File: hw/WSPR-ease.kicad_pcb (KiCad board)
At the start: 4 copper layers, 99 x 64 mm, 127 parts, among them J101 pwr+data, J102 SMA, J103 SMA, K201 G6K-2, K202 G6K-2, K203 G6K-2, Q101 MMBF170, Q201 MMBF170, Q202 MMBF170, Q203 MMBF170, Q301 MMBF170, Q302 MMBF170, Q303 MMBF170, Q304 MMBF170, Q305 MMBF170, Q306 MMBF170, Q307 MMBF170, Q308 MMBF170, T301 BN-43-202_DualPri_CTSec, U101 SRV05-4, U102 ESP32-S3-WROOM-1-N8R8, U103 LMR51430YDDCR, U104 GNSS module, U301 SN74LVC1G74DCTR, U302 UCC27525DGN, U303 UCC27525DGN, U304 Si5351C-B-GM1, Y301 40MHz

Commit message: Now using RP2040 as a DDS. I can use SPI co-host to program its (SPI) flash. I can use I2C between ESP32 and RP2040 to send commands and receive status.
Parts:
- removed the C304 at (81.4, 115.0)
- removed the C306 at (80.9, 113.7)
- removed the R302 at (77.1, 113.0)
- removed the U301 at (85.4, 113.0)
- added C401: 1uF X5R 25V, Capacitor_SMD:C_0402_1005Metric, F.Cu at (104.3, 108.5)
- added C402: 100nF X7R 50V, Capacitor_SMD:C_0402_1005Metric, F.Cu at (105.3, 108.5)
- added C403: 100pF NP0 50V, Capacitor_SMD:C_0402_1005Metric, F.Cu at (106.3, 108.5)
- added C404: 1uF X5R 25V, Capacitor_SMD:C_0402_1005Metric, F.Cu at (107.0, 102.2)
- added C405: 100nF X7R 50V, Capacitor_SMD:C_0402_1005Metric, F.Cu at (108.0, 102.2)
- added C406: 100nF X7R 50V, Capacitor_SMD:C_0402_1005Metric, F.Cu at (94.6, 98.3)
- added C407: 56pF NP0 50V, Capacitor_SMD:C_0402_1005Metric, F.Cu at (83.2, 97.0)
- added C408: 82pF NP0 50V, Capacitor_SMD:C_0402_1005Metric, F.Cu at (83.2, 94.8)
- added C409: 56pF NP0 50V, Capacitor_SMD:C_0402_1005Metric, F.Cu at (94.7, 100.5)
- added C410: 100nF X7R 50V, Capacitor_SMD:C_0402_1005Metric, F.Cu at (72.8, 109.5)
- added C411: 100nF X7R 50V, Capacitor_SMD:C_0402_1005Metric, F.Cu at (83.2, 108.6)
- added C412: 1uF X5R 25V, Capacitor_SMD:C_0402_1005Metric, F.Cu at (83.2, 111.2)
- added C413: 1uF X5R 25V, Capacitor_SMD:C_0402_1005Metric, F.Cu at (83.2, 112.1)
- added C414: 100nF X7R 50V, Capacitor_SMD:C_0402_1005Metric, F.Cu at (81.5, 104.0)
- added C415: 100nF X7R 50V, Capacitor_SMD:C_0402_1005Metric, F.Cu at (77.0, 103.7)
- added C416: 100nF X7R 50V, Capacitor_SMD:C_0402_1005Metric, F.Cu at (73.0, 108.5)
- added C417: 100nF X7R 50V, Capacitor_SMD:C_0402_1005Metric, F.Cu at (77.0, 113.8)
- added C418: 100nF X7R 50V, Capacitor_SMD:C_0402_1005Metric, F.Cu at (80.2, 113.8)
- added C419: 100nF X7R 50V, Capacitor_SMD:C_0402_1005Metric, F.Cu at (81.5, 113.5)
- added C420: 100nF X7R 50V, Capacitor_SMD:C_0402_1005Metric, F.Cu at (83.2, 110.2)
- added C421: 100nF X7R 50V, Capacitor_SMD:C_0402_1005Metric, F.Cu at (83.9, 117.0)
- added FB401: 600, Inductor_SMD:L_0603_1608Metric, F.Cu at (105.7, 106.8)
- added L401: 1.2uH, Inductor_SMD:L_1008_2520Metric, F.Cu at (85.5, 95.9)
- added L402: 1.2uH, Inductor_SMD:L_1008_2520Metric, F.Cu at (92.2, 100.3)
- added R401: 22.1k, Resistor_SMD:R_0402_1005Metric, F.Cu at (104.9, 105.0)
- added R402: 100, Resistor_SMD:R_0402_1005Metric, F.Cu at (75.0, 98.4)
- added R403: 100, Resistor_SMD:R_0402_1005Metric, F.Cu at (76.9, 98.4)
- added R404: 100, Resistor_SMD:R_0402_1005Metric, F.Cu at (78.8, 98.4)
- added R405: 100, Resistor_SMD:R_0402_1005Metric, F.Cu at (80.7, 98.4)
- added R406: 100, Resistor_SMD:R_0402_1005Metric, F.Cu at (82.6, 98.4)
- added R407: 100, Resistor_SMD:R_0402_1005Metric, F.Cu at (84.5, 98.4)
- added R408: 100, Resistor_SMD:R_0402_1005Metric, F.Cu at (86.4, 98.4)
- added R409: 200, Resistor_SMD:R_0402_1005Metric, F.Cu at (75.5, 100.7)
- added R410: 200, Resistor_SMD:R_0402_1005Metric, F.Cu at (76.5, 100.7)
- added R411: 200, Resistor_SMD:R_0402_1005Metric, F.Cu at (77.5, 100.7)
- added R412: 200, Resistor_SMD:R_0402_1005Metric, F.Cu at (78.5, 100.7)
- added R413: 200, Resistor_SMD:R_0402_1005Metric, F.Cu at (79.5, 100.7)
- added R414: 200, Resistor_SMD:R_0402_1005Metric, F.Cu at (80.5, 100.7)
- added R415: 200, Resistor_SMD:R_0402_1005Metric, F.Cu at (81.5, 100.7)
- added R416: 200, Resistor_SMD:R_0402_1005Metric, F.Cu at (82.5, 100.7)
- added R417: 200, Resistor_SMD:R_0402_1005Metric, F.Cu at (83.5, 100.7)
- added R418: 200, Resistor_SMD:R_0402_1005Metric, F.Cu at (92.7, 98.3)
- added R419: 22.1k, Resistor_SMD:R_0402_1005Metric, F.Cu at (104.9, 103.1)
- added TP401: GPIO8, TestPoint:TestPoint_Pad_1.5x1.5mm, F.Cu at (73.0, 103.3)
- added TP402: SWDIO, TestPoint:TestPoint_Bridge_Pitch2.0mm_Drill0.7mm, F.Cu at (76.0, 120.3)
- added TP403: SWCLK, TestPoint:TestPoint_Bridge_Pitch2.0mm_Drill0.7mm, F.Cu at (73.5, 120.3)
- added U401: 74LVC1G04, Package_TO_SOT_SMD:SOT-553, F.Cu at (106.6, 104.2)
- added U402: RP2040, Package_DFN_QFN:QFN-56-1EP_7x7mm_P0.4mm_EP3.2x3.2mm, F.Cu at (78.0, 108.8)
- added U403: W25Q128JVS, Package_SO:SOIC-8_5.3x5.3mm_P1.27mm, F.Cu at (89.5, 115.1)
- C101, C103, C110, C205, C206, C207, C208, C209, C210, C211, C212, C302, C307, C309: footprint Capacitor_SMD:C_0603_1608Metric -> Capacitor_SMD:C_0402_1005Metric
- C108, C303, C308: value 100pF NP0 100V -> 100pF NP0 50V; footprint Capacitor_SMD:C_0603_1608Metric -> Capacitor_SMD:C_0402_1005Metric
- C201, C204: value 910pF NP0 100V -> 910pF NP0 50V; footprint Capacitor_SMD:C_0603_1608Metric -> Capacitor_SMD:C_0402_1005Metric
- C202, C203: value 1.6nF NP0 63V -> 1.6nF NP0 25V; footprint Capacitor_SMD:C_0603_1608Metric -> Capacitor_SMD:C_0402_1005Metric
- C305: renamed from C312; footprint Capacitor_SMD:C_0603_1608Metric -> Capacitor_SMD:C_0402_1005Metric
- C312: renamed from C316; footprint Capacitor_SMD:C_0603_1608Metric -> Capacitor_SMD:C_0402_1005Metric
- C317: renamed from C319; footprint Capacitor_SMD:C_0603_1608Metric -> Capacitor_SMD:C_0402_1005Metric
- C319: renamed from C321; footprint Capacitor_SMD:C_0603_1608Metric -> Capacitor_SMD:C_0402_1005Metric
- C321: renamed from C323; footprint Capacitor_SMD:C_0603_1608Metric -> Capacitor_SMD:C_0402_1005Metric
- C323: renamed from C325; footprint Capacitor_SMD:C_0603_1608Metric -> Capacitor_SMD:C_0402_1005Metric
- C325: renamed from C327; footprint Capacitor_SMD:C_0603_1608Metric -> Capacitor_SMD:C_0402_1005Metric
- Y301: value 40MHz -> 12MHz; footprint Library:ECSTXO201633400TR -> Library:Oscillator_SMD_AbraconATX-H12-4Pin_2.5x2.0mm
- moved C304 26.2 mm to (73.1, 95.9)
- moved C305 26.2 mm to (74.4, 95.3)
- moved Y301 26.2 mm to (72.5, 98.8)
- moved R103 12.0 mm to (61.9, 125.7)
- moved R104 11.5 mm to (60.2, 126.1)
- moved C106 11.1 mm to (59.2, 126.1)
- moved R305 4.78 mm to (90.4, 109.8)
- moved R306 4.78 mm to (90.4, 108.5)
- moved C318 4.60 mm to (91.9, 104.6)
- moved C317 4.30 mm to (92.9, 104.6)
- moved C325 4.28 mm to (94.4, 104.4)
- moved C324 4.27 mm to (95.9, 111.2)
- moved C319 4.27 mm to (97.3, 108.5)
- moved C320 4.27 mm to (96.7, 109.8)
- moved C321 4.27 mm to (97.4, 106.7)
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- renumbered C311 to C304, C305 to C306, C313 to C311, C314 to C313, C315 to C314, C317 to C315, C318 to C316, C320 to C318, C322 to C320, C324 to C322, C326 to C324, C328 to C326, R303 to R302, R304 to R303, R305 to R304, R306 to R305, R307 to R306, U302 to U301, U303 to U302, U304 to U303
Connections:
- U102 pad 15: unconnected-(U102-IO3-Pad15) -> /ddsRUN
- U102 pad 18: /txCLKen -> unconnected-(U102-IO10-Pad18)
- U102 pad 19: /tcxoDiv2 -> /ddsClk
- U102 pad 22: unconnected-(U102-IO14-Pad22) -> /ddsSPI.D3
- U102 pad 23: unconnected-(U102-IO21-Pad23) -> /ddsSPI.SCK
- U102 pad 24: unconnected-(U102-IO47-Pad24) -> /ddsSPI.D0
- U102 pad 25: unconnected-(U102-IO48-Pad25) -> /ddsSPI.D2
- U102 pad 26: /ahcEn -> /ddsSPI.D1
- U102 pad 27: unconnected-(U102-IO0-Pad27) -> /ddsSPI.SS
- U102 pad 38: unconnected-(U102-IO2-Pad38) -> /ahcEn
- U303 pad 6: /Transmitter/tcxo -> /Transmitter/DDS/out
- Y301 pad 3: /Transmitter/tcxo -> /ddsClk
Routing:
- net /ddsSPI.D1: track 0.00 -> 38.3 mm, vias 0 -> 3
- net /ddsSPI.SS: track 0.00 -> 35.7 mm, vias 0 -> 3
- net /ddsSPI.D2: track 0.00 -> 32.1 mm, vias 0 -> 3
- net /ddsSPI.D0: track 0.00 -> 25.5 mm, vias 0 -> 3
- net /ddsSPI.D3: track 0.00 -> 24.5 mm, vias 0 -> 3
- net /ddsClk: track 0.00 -> 23.9 mm
- net /ddsSPI.SCK: track 0.00 -> 23.5 mm, vias 0 -> 3
- net +3.3V: track 46.0 -> 68.9 mm, vias 22 -> 32
- net /ahcEn: track 36.7 -> 58.8 mm, vias 0 -> 2
- net /Transmitter/DDS/out: track 0.00 -> 19.8 mm, vias 0 -> 2
- net Net-(C406-Pad2): track 0.00 -> 15.4 mm, vias 0 -> 2
- net /tcxoDiv2: track 15.0 -> 0.00 mm
- net /txCLKen: track 14.8 -> 0.00 mm
- net +1.1V: track 0.00 -> 14.0 mm
- net Net-(Q101-S): track 20.2 -> 6.68 mm
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
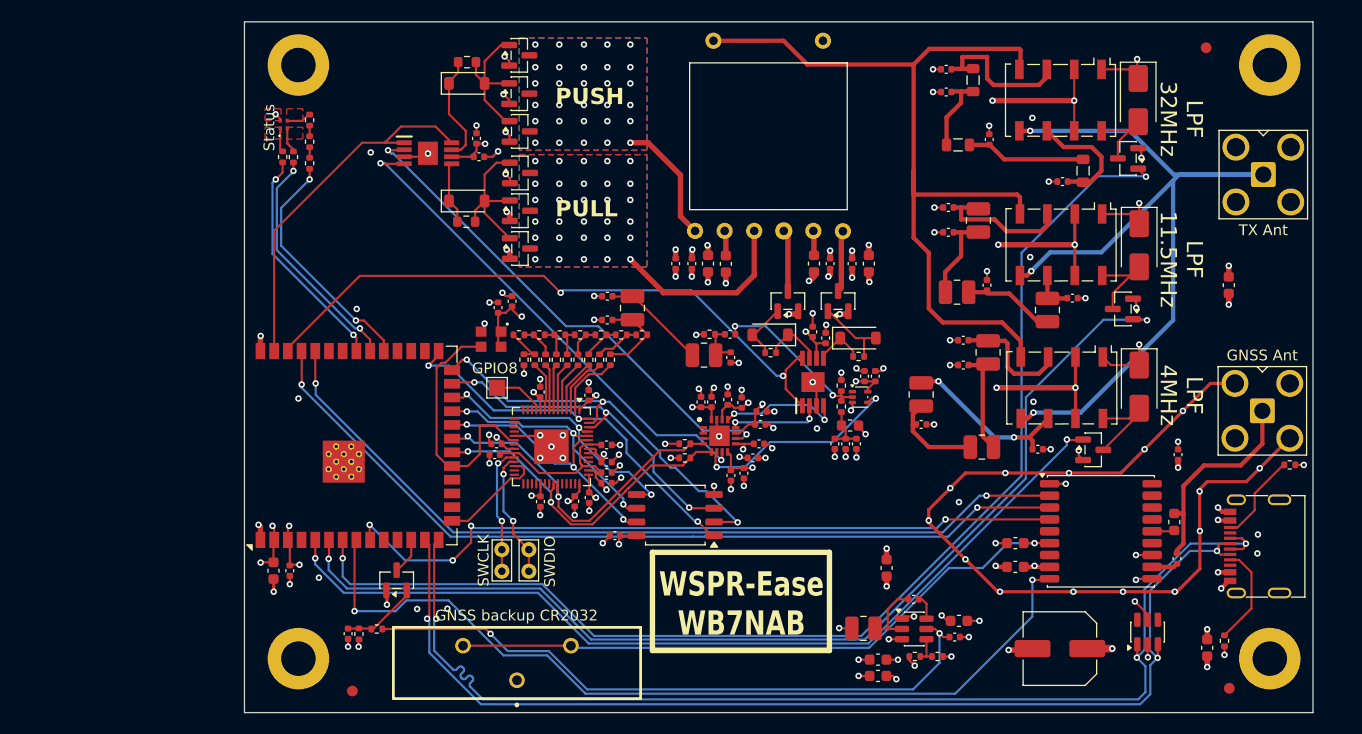
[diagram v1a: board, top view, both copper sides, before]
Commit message: Switched to SI5351 clocking MACHXO2 CPLD to drive gate driver for MOSFETs. It passes DRC but needs serious reviewing.
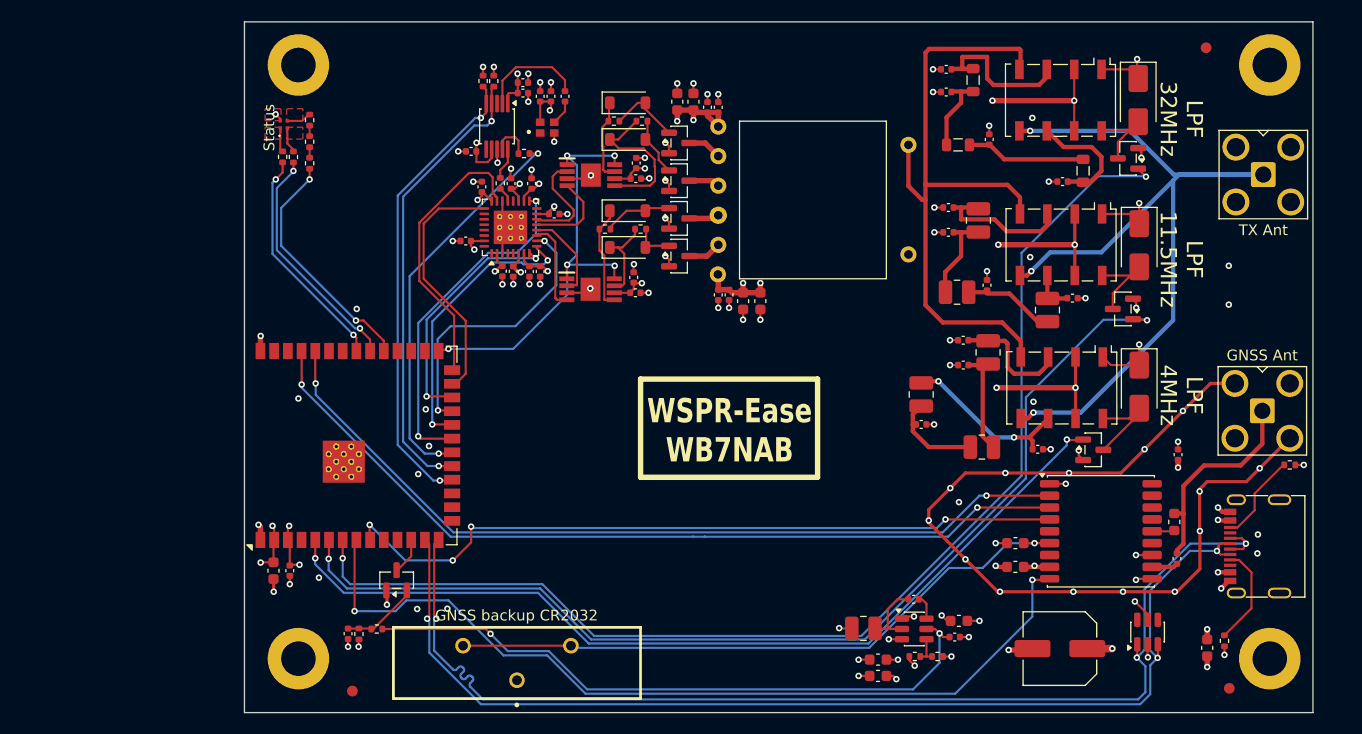
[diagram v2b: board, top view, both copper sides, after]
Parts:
- removed the C302 at (91.0, 91.8)
- removed the C305 at (74.4, 95.3)
- removed the C309 at (103.9, 91.8)
- removed C313, C314, C315, C316: 10uF X5R 25V, Capacitor_SMD:C_0603_1608Metric
- removed C317, C319, C321, C323, C325, C414, C419, C420, C421: 100nF X7R 50V, Capacitor_SMD:C_0402_1005Metric
- removed C318, C320, C322, C324, C326, C412, C413: 1uF X5R 25V, Capacitor_SMD:C_0402_1005Metric
- removed FB401: 600, Inductor_SMD:L_0603_1608Metric
- removed L401, L402: 1.2uH, Inductor_SMD:L_1008_2520Metric
- removed Q305, Q306, Q307, Q308: MMBF170, Package_TO_SOT_SMD:SOT-23
- removed R305, R306: 5.1k, Resistor_SMD:R_0402_1005Metric
- removed R405, R406, R407, R408: 100, Resistor_SMD:R_0402_1005Metric
- removed R409, R410, R411, R412, R413, R414, R415, R416, R417, R418: 200, Resistor_SMD:R_0402_1005Metric
- removed R419: 22.1k, Resistor_SMD:R_0402_1005Metric
- removed TP401: GPIO8, TestPoint:TestPoint_Pad_1.5x1.5mm
- removed TP402: SWDIO, TestPoint:TestPoint_Bridge_Pitch2.0mm_Drill0.7mm
- removed TP403: SWCLK, TestPoint:TestPoint_Bridge_Pitch2.0mm_Drill0.7mm
- removed U303: Si5351C-B-GM1, Library:QFN50P300X300X90-17N-D
- removed U403: W25Q128JVS, Package_SO:SOIC-8_5.3x5.3mm_P1.27mm
- removed Y301: 12MHz, Library:Oscillator_SMD_AbraconATX-H12-4Pin_2.5x2.0mm
- added C306: 100pF NP0 50V, Capacitor_SMD:C_0402_1005Metric, F.Cu at (93.5, 77.3)
- added C307: 100pF NP0 50V, Capacitor_SMD:C_0402_1005Metric, F.Cu at (93.5, 94.7)
- added C312: 10uF X5R 25V, Capacitor_SMD:C_0603_1608Metric, F.Cu at (95.8, 95.3)
- added Y401: 20MHz, Library:ECSTXO201633400TR, F.Cu at (77.7, 79.2)
- C303: value 100pF NP0 50V -> 10uF X5R 25V; footprint Capacitor_SMD:C_0402_1005Metric -> Capacitor_SMD:C_0603_1608Metric
- C304, C401, C404: value 1uF X5R 25V -> 100nF X7R 50V
- C308, C403: value 100pF NP0 50V -> 100nF X7R 50V
- C407: value 56pF NP0 50V -> 1uF X5R 25V
- C408: value 82pF NP0 50V -> 1uF X5R 25V
- C409: value 56pF NP0 50V -> 100nF X7R 50V
- C417: value 100nF X7R 50V -> 1uF X5R 25V
- D301, D302, D303, D304: value 1N4148W -> BAT54FILM
- Q101, Q201, Q202, Q203, Q301, Q302, Q303, Q304: value MMBF170 -> IRLML2060
- R301, R302: value 10 -> 27; footprint Resistor_SMD:R_0603_1608Metric -> Resistor_SMD:R_0402_1005Metric
- R303, R304: value 47 -> 27
- R401: value 22.1k -> 27
- R402, R403: value 100 -> 5.1k
- R404: value 100 -> 27
- U301, U302: value UCC27525DGN -> UCC27523DGN
- U401: value 74LVC1G04 -> LCMXO2-256HC-4SG32C; footprint Package_TO_SOT_SMD:SOT-553 -> Package_DFN_QFN:QFN-32-1EP_5x5mm_P0.5mm_EP3.1x3.1mm_ThermalVias
- U402: value RP2040 -> SI5351A-B-GT; footprint Package_DFN_QFN:QFN-56-1EP_7x7mm_P0.4mm_EP3.2x3.2mm -> Package_SO:MSOP-10_3x3mm_P0.5mm
- moved C402 39.9 mm to (70.1, 89.7), turned to 0 degrees
- moved C404 39.6 mm to (71.6, 84.7), turned to -90 degrees
- moved R401 37.8 mm to (73.3, 84.4), turned to 90 degrees
- moved C418 37.7 mm to (77.0, 76.3), turned to 90 degrees
- moved C417 37.6 mm to (78.0, 76.3), turned to 90 degrees
- moved C401 37.0 mm to (76.2, 84.4)
- moved C403 36.5 mm to (73.5, 92.5)
- moved U401 36.0 mm to (74.2, 88.4), turned to 90 degrees
- moved C405 33.5 mm to (76.0, 92.5)
- moved C409 31.2 mm to (75.4, 76.0), turned to 180 degrees
- moved U402 30.1 mm to (73.0, 79.1)
- moved C415 27.5 mm to (79.3, 76.3)
- moved C304 26.9 mm to (92.5, 77.3)
- moved C416 24.2 mm to (74.3, 84.4), turned to -90 degrees
- moved R403 23.9 mm to (72.7, 74.9), turned to 90 degrees
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- renumbered C306 to C302, C307 to C305, C311 to C309, C312 to C311, R110 to R105, R111 to R106, R105 to R107, R106 to R108, R107 to R109, R108 to R110, R109 to R111
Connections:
- C301 pad 1: GND -> VBUS
- C301 pad 2: VBUS -> GND
- C303 pad 1: GND -> VBUS
- C303 pad 2: VBUS -> GND
- C304 pad 1: +3.3V -> VBUS
- C308 pad 1: GND -> VBUS
- C308 pad 2: VBUS -> GND
- C310 pad 1: GND -> VBUS
- C310 pad 2: VBUS -> GND
- C401 pad 1: +VDDA -> GND
- C401 pad 2: GND -> +3.3V
- C402 pad 1: +VDDA -> GND
- C402 pad 2: GND -> +3.3V
- C403 pad 2: +VDDA -> +3.3V
- C404 pad 1: +3.3V -> GND
- C404 pad 2: GND -> +3.3V
- C405 pad 1: +3.3V -> GND
- C405 pad 2: GND -> +3.3V
- C406 pad 1: Net-(C406-Pad1) -> GND
- C406 pad 2: Net-(C406-Pad2) -> +3.3V
- C407 pad 1: GND -> +3.3V
- C407 pad 2: Net-(C407-Pad2) -> GND
- C408 pad 1: GND -> +3.3V
- C408 pad 2: Net-(C408-Pad2) -> GND
- C409 pad 2: Net-(C406-Pad1) -> +3.3V
- C410 pad 1: +1.1V -> GND
- C410 pad 2: GND -> +3.3V
- C411 pad 1: +1.1V -> GND
- C411 pad 2: GND -> +3.3V
- C415 pad 1: +3.3V -> Net-(Y401-OUTPUT)
- C415 pad 2: GND -> Net-(U402-XA)
- C416 pad 1: +3.3V -> GND
- C416 pad 2: GND -> +3.3V
- Q301 pad 3: /Transmitter/txPullT -> /Transmitter/pushPeakT
- Q302 pad 1: Net-(D301-A) -> Net-(D302-A)
- Q302 pad 3: /Transmitter/txPullT -> /Transmitter/pushBaseT
- Q303 pad 1: Net-(D301-A) -> Net-(D303-A)
- Q303 pad 3: /Transmitter/txPullT -> /Transmitter/pullBaseT
- Q304 pad 1: Net-(D302-A) -> Net-(D304-A)
- Q304 pad 3: /Transmitter/txPushT -> /Transmitter/pullPeakT
- R401 pad 1: Net-(C406-Pad2) -> Net-(U401B-PCLKT1_0)
- R401 pad 2: +VDDA -> Net-(U402-CLK0)
- R402 pad 1: Net-(R402-Pad1) -> /txSDA
- R402 pad 2: Net-(R402-Pad2) -> +3.3V
- R403 pad 1: Net-(R403-Pad1) -> /txSCL
- R403 pad 2: Net-(R402-Pad1) -> +3.3V
- R404 pad 1: Net-(R404-Pad1) -> /tcxo
- R404 pad 2: Net-(R403-Pad1) -> Net-(U402-CLK1)
- T301 pad 1: /Transmitter/ahcPushT -> VBUS
- T301 pad 2: VBUS -> /Transmitter/pullBaseT
- T301 pad 3: /Transmitter/ahcPullT -> /Transmitter/pullPeakT
- T301 pad 4: /Transmitter/txPullT -> /Transmitter/pushPeakT
- T301 pad 5: VBUS -> /Transmitter/pushBaseT
- T301 pad 6: /Transmitter/txPushT -> VBUS
- U102 pad 15: /ddsRUN -> unconnected-(U102-IO3-Pad15)
- U102 pad 18: unconnected-(U102-IO10-Pad18) -> /txSDA
- U102 pad 19: /ddsClk -> /txSCL
- U102 pad 20: /txSDA -> /tcxo
- U102 pad 21: /txSCL -> /cpldMOSI
- U102 pad 22: /ddsSPI.D3 -> /cpldSCK
- U102 pad 23: /ddsSPI.SCK -> /cpldMISO
- U102 pad 24: /ddsSPI.D0 -> /cpldNCS
- U102 pad 25: /ddsSPI.D2 -> /cpldPROG
- U102 pad 26: /ddsSPI.D1 -> /cpldDONE
- U102 pad 27: /ddsSPI.SS -> /paEn
- U102 pad 38: /ahcEn -> unconnected-(U102-IO2-Pad38)
- U102 pad 39: /txPAen -> unconnected-(U102-IO1-Pad39)
- U301 pad 1: /txPAen -> /paEn
- U301 pad 2: /Transmitter/txCLK1 -> /Transmitter/nPushBase
- U301 pad 4: /Transmitter/txCLK2 -> /Transmitter/nPushPeak
- U301 pad 8: /txPAen -> /paEn
- U302 pad 1: /ahcEn -> /paEn
- U302 pad 2: /Transmitter/ahcCLK2 -> /Transmitter/nPullBase
- U302 pad 4: /Transmitter/ahcCLK1 -> /Transmitter/nPullPeak
- U302 pad 5: Net-(D303-K) -> Net-(D304-K)
- U302 pad 7: Net-(D304-K) -> Net-(D303-K)
- U302 pad 8: /ahcEn -> /paEn
- U401 pad 2: Net-(C406-Pad2) -> +3.3V
- U401 pad 4: /Transmitter/DDS/out -> unconnected-(U401D-PCLKT3_0-Pad4)
- U401 pad 5: +3.3V -> unconnected-(U401D-PCLKC3_0-Pad5)
- U402 pad 10: +3.3V -> Net-(U402-CLK0)
- U402 pad 2: /Transmitter/DDS/dac0 -> Net-(U402-XA)
- U402 pad 3: /Transmitter/DDS/dac1 -> unconnected-(U402-XB-Pad3)
- U402 pad 4: /Transmitter/DDS/dac2 -> /txSCL
- U402 pad 5: /Transmitter/DDS/dac3 -> /txSDA
- U402 pad 6: /Transmitter/DDS/dac4 -> unconnected-(U402-CLK2-Pad6)
- U402 pad 7: /Transmitter/DDS/dac5 -> +3.3V
- U402 pad 8: /Transmitter/DDS/dac6 -> GND
- U402 pad 9: /Transmitter/DDS/dac7 -> Net-(U402-CLK1)
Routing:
- net /ahcEn: track 58.8 -> 0.00 mm, vias 2 -> 0
- net /Transmitter/txCLK1: track 46.7 -> 0.00 mm, vias 2 -> 0
- net /Transmitter/txCLK2: track 46.0 -> 0.00 mm, vias 2 -> 0
- net /paEn: track 0.00 -> 40.6 mm, vias 0 -> 5
- net /ddsSPI.D1: track 38.3 -> 0.00 mm, vias 3 -> 0
- net /tcxo: track 0.00 -> 36.8 mm, vias 0 -> 2
- net /ddsSPI.SS: track 35.7 -> 0.00 mm, vias 3 -> 0
- net /txPAen: track 34.0 -> 0.00 mm
- net /ddsSPI.D2: track 32.1 -> 0.00 mm, vias 3 -> 0
- net /cpldMOSI: track 0.00 -> 31.7 mm, vias 0 -> 2
- net /cpldMISO: track 0.00 -> 26.4 mm, vias 0 -> 2
- net /cpldSCK: track 0.00 -> 26.2 mm, vias 0 -> 2
- net /cpldDONE: track 0.00 -> 25.8 mm
- net GND: track 215.2 -> 189.5 mm, vias 141 -> 109
- net /ddsSPI.D0: track 25.5 -> 0.00 mm, vias 3 -> 0
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- removed copper zone on B.Cu, net /Transmitter/txPullT
- removed copper zone on F.Cu, net /Transmitter/txPullT
- removed copper zone on B.Cu, net /Transmitter/txPushT
- removed copper zone on F.Cu, net /Transmitter/txPushT
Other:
- board text removed: "PULL"
- board text removed: "PUSH"

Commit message: Various schematic clean ups. Improved/fixed decoupling around relays. Filter Vdd for TCXO and SI5351 to try to minimize modulation of the clock freq by noise
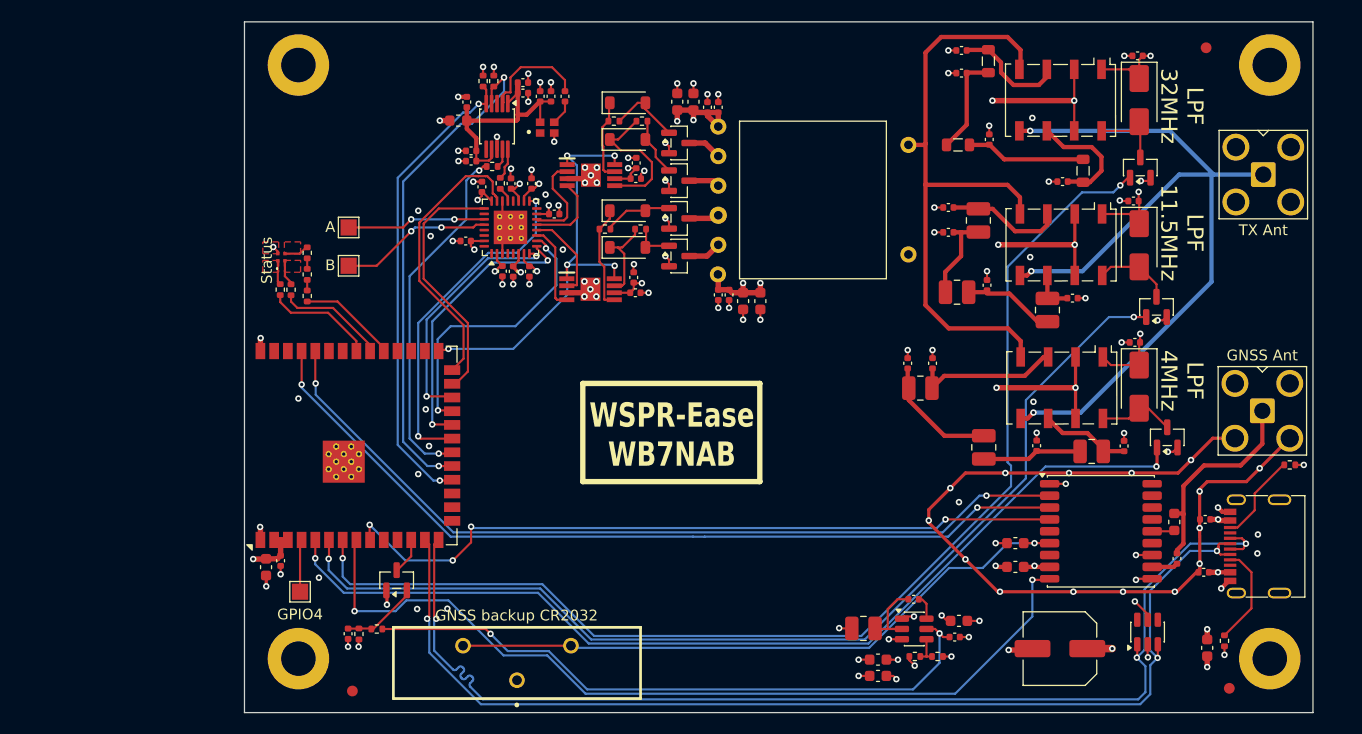
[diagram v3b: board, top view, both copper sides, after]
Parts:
- added C101: 100nF X7R 50V, Capacitor_SMD:C_0402_1005Metric, F.Cu at (138.5, 120.4)
- added C201: 1uF X5R 25V, Capacitor_SMD:C_0402_1005Metric, F.Cu at (132.1, 99.1)
- added C206: 1uF X5R 25V, Capacitor_SMD:C_0402_1005Metric, F.Cu at (132.0, 86.0)
- added C211: 1uF X5R 25V, Capacitor_SMD:C_0402_1005Metric, F.Cu at (132.3, 72.5)
- added C416: 1uF X5R 25V, Capacitor_SMD:C_0402_1005Metric, F.Cu at (70.2, 76.8)
- added FB401: 600@1A, Inductor_SMD:L_0603_1608Metric, F.Cu at (69.4, 78.5)
- added TP101: GPIO4, TestPoint:TestPoint_Pad_1.5x1.5mm, F.Cu at (54.8, 122.2)
- added TP401: A, TestPoint:TestPoint_Pad_1.5x1.5mm, F.Cu at (59.2, 88.5)
- added TP402: B, TestPoint:TestPoint_Pad_1.5x1.5mm, F.Cu at (59.2, 92.0)
- moved L203 16.7 mm to (128.1, 109.2), turned to 0 degrees
- moved D101 12.3 mm to (53.0, 91.2)
- moved R107 12.3 mm to (55.4, 94.8)
- moved R108 12.3 mm to (55.4, 92.8)
- moved R109 12.3 mm to (55.4, 90.8)
- moved R110 12.3 mm to (53.9, 94.2)
- moved R111 12.3 mm to (52.9, 94.2)
- moved C410 12.1 mm to (70.6, 82.3), turned to 0 degrees
- moved C204 10.9 mm to (123.0, 108.7), turned to 90 degrees
- moved C205 8.01 mm to (131.1, 108.7), turned to 90 degrees
- moved L201 7.09 mm to (112.2, 103.3), turned to 180 degrees
- moved Q201 6.96 mm to (135.1, 107.9), turned to 90 degrees
- moved C102 6.50 mm to (138.6, 115.5), turned to 180 degrees
- moved C203 5.15 mm to (111.0, 101.0), turned to 90 degrees
- moved C202 3.56 mm to (113.3, 101.0), turned to 90 degrees
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- renumbered C101 to C102, C102 to C103, C103 to C104, C104 to C105, C105 to C106, C106 to C107, C107 to C108, C108 to C109, C109 to C110, C110 to C111, C111 to C112, C112 to C113, C113 to C114, C114 to C115, C201 to C202, C202 to C203, C203 to C204, C204 to C205, C205 to C207, C206 to C208, C207 to C209, C208 to C210, C209 to C212, C210 to C213, C211 to C214, C212 to C215, C405 to C403, C406 to C404, C403 to C405, C404 to C406, C415 to C411, C416 to C412, C411 to C413, C417 to C414, C418 to C415, R404 to R402, R402 to R403, R403 to R404
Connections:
- C407 pad 1: +3.3V -> +VDDA
- C408 pad 1: +3.3V -> +VDDA
- C409 pad 2: +3.3V -> +VDDA
- C410 pad 2: +3.3V -> +VDDA
- C414 pad 1: +3.3V -> +VDDA
- C415 pad 1: +3.3V -> +VDDA
- R403 pad 1: /txSDA -> /txSCL
- R404 pad 1: /txSCL -> /txSDA
- U102 pad 4: unconnected-(U102-IO4-Pad4) -> Net-(U102-IO4)
- U401 pad 27: unconnected-(U401A-SDA/PCLKC0_0-Pad27) -> Net-(U401A-SDA/PCLKC0_0)
- U401 pad 28: unconnected-(U401A-SCL/PCLKT0_0-Pad28) -> Net-(U401A-SCL/PCLKT0_0)
- U402 pad 1: +3.3V -> +VDDA
- U402 pad 7: +3.3V -> +VDDA
- Y401 pad 4: +3.3V -> +VDDA
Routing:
- net +VDDA: track 0.00 -> 22.6 mm
- net +3.3V: track 52.3 -> 37.2 mm, vias 25 -> 20
- net Net-(U401A-SCL/PCLKT0_0): track 0.00 -> 14.1 mm, vias 0 -> 2
- net /hbRed: track 22.3 -> 8.87 mm, vias 2 -> 0
- net Net-(U401A-SDA/PCLKC0_0): track 0.00 -> 12.9 mm, vias 0 -> 2
- net /hbGrn: track 21.9 -> 9.58 mm, vias 2 -> 0
- net /hbBlu: track 21.1 -> 10.1 mm, vias 2 -> 0
- net Net-(C205-Pad1): track 15.7 -> 8.19 mm, vias 2 -> 0
- net /loON: track 84.7 -> 91.8 mm
- net Net-(U102-IO4): track 0.00 -> 4.66 mm
- net /tcxo: track 36.8 -> 32.8 mm
- net /txSCL: track 42.6 -> 46.5 mm
- net VBUS: track 107.3 -> 111.2 mm, vias 19 -> 17
- net Net-(C212-Pad1): track 13.9 -> 9.99 mm
- net Net-(C202-Pad1): track 10.2 -> 13.7 mm
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
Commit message: Simplify. Put exciter stuff onto transmitter sheet.
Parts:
- renumbered C401 to C301, C402 to C302, C405 to C303, C406 to C304, C301 to C305, C302 to C306, C303 to C307, C304 to C308, C305 to C309, C306 to C310, C404 to C311, C403 to C312, C307 to C313, C308 to C314, C309 to C315, C310 to C316, C311 to C317, C312 to C318, C416 to C319, C407 to C320, C408 to C321, C413 to C322, C409 to C323, C410 to C324, C411 to C325, C412 to C326, C414 to C327, C415 to C328, FB401 to FB301, R401 to R305, R402 to R306, R403 to R307, R404 to R308, TP401 to TP301, TP402 to TP302, U401 to U301, U301 to U302, U302 to U303, U402 to U304, Y401 to Y301
